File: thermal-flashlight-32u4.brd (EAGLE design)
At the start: 49.8 x 42.9 mm, 31 parts, among them IC1 ATMEGA328P, IC2 MCP73831, IC4 MCP1700-33, J1 AYZ0202, J2 1X2-3.5MM, Q4 BSS123, U1 MLX90614_, X1 USBSMD

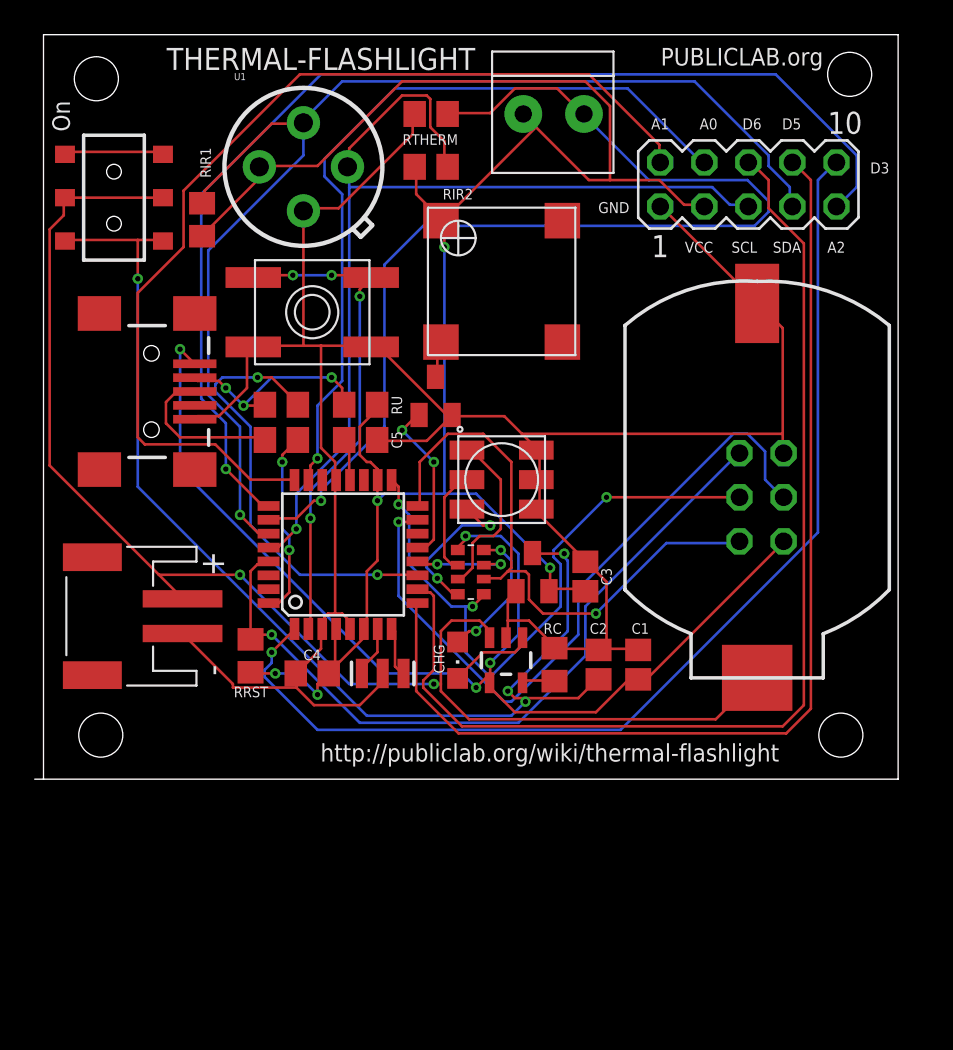
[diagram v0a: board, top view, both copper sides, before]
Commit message: added 32u4
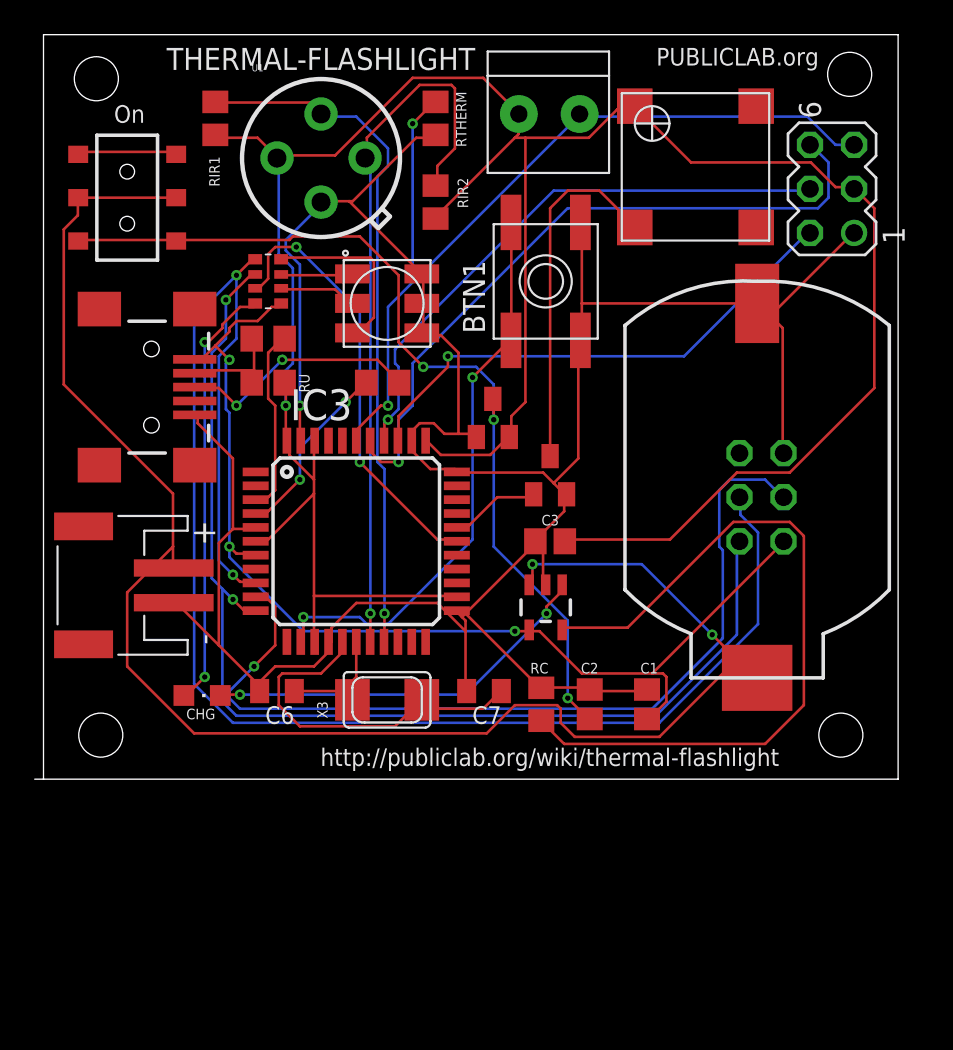
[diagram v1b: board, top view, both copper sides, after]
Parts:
- removed BTN: (no value), adafruit:EVQ-Q2
- removed C4, C5: 0.1uF, rcl:C0805
- removed IC1: ATMEGA328P, atmel:TQFP32-08
- removed RRST: 10k, rcl:R0805@1
- removed X: 12MHz, SparkFunNew:RESONATOR-SMD
- added BTN1: (no value), adafruit:EVQ-Q2
- added C6, C7: 18pF, adafruit:C0805K
- added IC3: ATMEGA32U4-AU, adaprog:TQFP44
- added X3: 8MHz, adaprog:NX5032
- SV1: device con-lstb:MA05-2 -> con-lstb:MA03-2
- moved RN1 20.4 mm to (13.2, 28.7), turned to 270 degrees
- moved CHG 14.9 mm to (9.40, 4.83), turned to 270 degrees
- moved U$1 13.0 mm to (37.8, 35.3)
- moved LED 12.1 mm to (20.1, 27.4)
- moved IC4 9.18 mm to (26.2, 20.8)
- moved Q4 8.03 mm to (29.5, 17.5)
- moved RD+ 6.71 mm to (19.8, 22.9), turned to 180 degrees
- moved RIR1 5.89 mm to (10.2, 38.1)
- moved RU 5.48 mm to (13.2, 22.9)
- moved SV1 4.83 mm to (45.7, 34.0), turned to 90 degrees
- moved RD- 3.89 mm to (13.2, 25.4)
- moved IC2 3.81 mm to (29.2, 9.91)
- moved C3 2.87 mm to (29.5, 13.7), turned to 180 degrees
- moved RC 2.41 mm to (29.0, 4.32)
- moved C1 2.34 mm to (35.1, 4.32)
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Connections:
- removed net AREF: C5.2, IC1.20
- removed net D10: IC1.14
- removed net D2: IC1.32, RD+.2
- removed net D3: IC1.1, SV1.10
- removed net D4: BTN.B, BTN.B', IC1.2
- removed net D5: IC1.9, SV1.8
- removed net D6: IC1.10, SV1.6
- removed net N$12: IC1.19
- removed net N$13: IC1.22
- removed net N$2: IC1.7, X.1
- removed net N$3: IC1.8, X.3
- removed net RXD: IC1.30
- removed net TXD: IC1.31
- new net A4: IC3.40
- new net A5: IC3.41
- new net D0/RX: IC3.20
- new net D1/TX: IC3.21
- new net D11: IC3.12
- new net D4_A6: IC3.25
- new net D6*: IC3.27
- new net IO10*: IC3.30
- new net IO12*: IC3.26
- new net N$11: IC3.4, RD+.2
- new net N$15: C7.1, IC3.16, X3.P$1
- new net N$16: C6.1, IC3.17, X3.P$2
- new net N$18: IC3.3, RD-.2
- new net PC6: IC3.31
- new net PC7: IC3.32
- new net RST: BTN1.B, BTN1.B', IC3.13
- new net RXLED/SS: IC3.8
- new net TXLED: IC3.22
- net A0: now also IC3.36, SV1.2; no longer IC1.23, SV1.4
- net A1: now also IC3.37, SV1.4; no longer IC1.24, SV1.2
- net A2: now also IC3.38, SV1.6; no longer IC1.25, SV1.9
- net A3: now also IC3.39, SV1.5; no longer IC1.26
- net D7: now also IC3.1; no longer IC1.11, RD-.2
- net D8: now also IC3.28; no longer IC1.12
- net D9: now also IC3.29; no longer IC1.13
- net GND: now also BTN1.A, BTN1.A', C6.2, C7.2, IC3.15, IC3.23, IC3.33, IC3.35, IC3.43, IC3.5; no longer BTN.A, BTN.A', C4.1, C5.1, IC1.21, IC1.3, IC1.5, X.2
- net MISO: now also IC3.11; no longer IC1.16
- net MOSI: now also IC3.10; no longer IC1.15
- net RESET: no longer IC1.29, RRST.1
- net SCK: now also IC3.9; no longer IC1.17
- net SCL: now also IC3.18; no longer IC1.28, SV1.5
- net SDA: now also IC3.19; no longer IC1.27, SV1.7
- net VBUS: now also IC3.7
- net VCC: now also IC3.14, IC3.24, IC3.34, IC3.42, IC3.44, IC3.6; no longer C4.2, IC1.18, IC1.4, IC1.6, RRST.2
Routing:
- net D3: track 63.2 -> 0.00 mm, vias 1 -> 0
- net D6: track 62.7 -> 0.00 mm
- net D5: track 61.4 -> 0.00 mm
- net SCK: track 36.5 -> 89.2 mm, vias 3 -> 2
- net RESET: track 43.7 -> 0.00 mm, vias 1 -> 0
- net N$6: track 1.90 -> 43.2 mm
- net VCC: track 115.3 -> 153.7 mm, vias 5 -> 1
- net RST: track 0.00 -> 32.8 mm, vias 0 -> 2
- net MISO: track 34.1 -> 65.9 mm, vias 1 -> 2
- net SDA: track 69.1 -> 40.1 mm
- net D4: track 28.8 -> 0.00 mm, vias 4 -> 0
- net A2: track 65.9 -> 40.0 mm
- net D7: track 25.4 -> 0.00 mm, vias 2 -> 0
- net GND: track 142.3 -> 167.3 mm, vias 0 -> 1
- net A1: track 58.3 -> 33.4 mm, vias 0 -> 1
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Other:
- board text removed: "A0"
- board text removed: "A1"
- board text removed: "A2"
- board text removed: "D3"
- board text removed: "D5"
- board text removed: "D6"
- board text removed: "GND"
- board text removed: "SCL"
- board text removed: "SDA"
- board text removed: "VCC"

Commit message: update
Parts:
- renumbered BTN1 to BTN
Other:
- board text added: "buzzer"
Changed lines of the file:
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@@
 <circle x="46.736" y="40.64" radius="1.27" width="0.002540625" layer="20"/>
 <circle x="46.228" y="2.54" radius="1.27" width="0.002540625" layer="20"/>
+<text x="40.386" y="35.052" size="0.8128" layer="25" ratio="20" rot="R180">buzzer</text>
 </plain>
 <attributes>
@@
 <element name="C7" library="adafruit" package="C0805K" value="18pF" x="25.654" y="5.08" rot="R180"/>
 <element name="IC3" library="adaprog" package="TQFP44" value="ATMEGA32U4-AU" x="18.288" y="13.716"/>
-<element name="BTN1" library="adafruit" package="EVQ-Q2" value="" x="29.21" y="28.702" rot="R90"/>
+<element name="BTN" library="adafruit" package="EVQ-Q2" value="" x="29.21" y="28.702" smashed="yes" rot="R90">
+<attribute name="NAME" x="25.71" y="25.702" size="0.8128" layer="25" rot="R90"/>
+<attribute name="VALUE" x="34.01" y="25.502" size="1.27" layer="27" rot="R90"/>
+</element>
 <element name="SV1" library="con-lstb" package="MA03-2" value="" x="45.72" y="34.036" smashed="yes" rot="R90">
 <attribute name="OC_NEWARK" value="unknown" x="45.72" y="34.036" size="1.778" layer="27" rot="R90" display="off"/>
@@
 <contactref element="C7" pad="2"/>
 <contactref element="IC3" pad="33"/>
-<contactref element="BTN1" pad="A'"/>
-<contactref element="BTN1" pad="A"/>
+<contactref element="BTN" pad="A'"/>
+<contactref element="BTN" pad="A"/>
 <contactref element="SV1" pad="1"/>
 <wire x1="31.2928" y1="31.9024" x2="31.2928" y2="27.432" width="0.1524" layer="1"/>
@@
 <signal name="RST">
 <contactref element="IC3" pad="13"/>
-<contactref element="BTN1" pad="B"/>
-<contactref element="BTN1" pad="B'"/>
+<contactref element="BTN" pad="B"/>
+<contactref element="BTN" pad="B'"/>
 <wire x1="15.24" y1="9.3472" x2="15.24" y2="7.9248" width="0.1524" layer="1"/>
 <wire x1="18.4912" y1="9.3472" x2="15.24" y2="9.3472" width="0.1524" layer="16"/>

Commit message: update
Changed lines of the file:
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@@
 <text x="42.672" y="1.778" size="1.016" layer="25" ratio="20" rot="R180">http://publiclab.org/wiki/thermal-flashlight</text>
 <text x="25.146" y="42.164" size="1.27" layer="25" ratio="20" rot="R180">THERMAL-FLASHLIGHT</text>
-<text x="44.958" y="42.164" size="1.016" layer="25" ratio="20" rot="R180">PUBLICLAB.org</text>
+<text x="44.704" y="41.91" size="1.016" layer="25" ratio="20" rot="R180">PUBLICLAB.org</text>
 <wire x1="49.53" y1="0" x2="0.254" y2="0" width="0" layer="20"/>
 <wire x1="0.254" y1="0" x2="-0.254" y2="0" width="0" layer="20"/>

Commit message: update
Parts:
- added LED1: RGBLED5050, adafruit:RGBLED5050
- added RN2: (no value), resistor-dil:EXB38V
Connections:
- new net N$12: LED1.2, RN2.6
- new net N$2: LED1.3, RN2.8
- new net N$3: LED1.1, RN2.7
- net A3: no longer J2.2, RTHERM.2
- net A4: now also J2.2, RTHERM.2
- net D8: now also RN2.3
- net GND: now also LED1.4, LED1.5, LED1.6
- net MISO: now also RN2.2
- net SCK: now also RN2.1
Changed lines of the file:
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@@
 <attribute name="VALUE" x="49.911" y="32.766" size="1.27" layer="27" ratio="10" rot="R90"/>
+</element>
+<element name="LED1" library="adafruit" package="RGBLED5050" value="RGBLED5050" x="3.048" y="-4.826"/>
+<element name="RN2" library="resistor-dil" package="EXB38V" value="" x="2.286" y="-12.446">
+<attribute name="OC_NEWARK" value="unknown" x="-6.35" y="-3.048" size="1.778" layer="27" display="off"/>
+<attribute name="MPN" value="" x="-6.35" y="-3.048" size="1.778" layer="27" display="off"/>
+<attribute name="MF" value="" x="-6.35" y="-3.048" size="1.778" layer="27" display="off"/>
+<attribute name="OC_FARNELL" value="unknown" x="-6.35" y="-3.048" size="1.778" layer="27" display="off"/>
 </element>
 </elements>
@@
 <wire x1="31.0896" y1="25.1968" x2="31.21" y2="25.302" width="0.1524" layer="1"/>
 <via x="15.0368" y="21.5392" extent="1-16" drill="0.3048"/>
+<contactref element="LED1" pad="4"/>
+<contactref element="LED1" pad="6"/>
+<contactref element="LED1" pad="5"/>
+<wire x1="5.048" y1="-3.126" x2="12.5984" y2="5.08" width="0" layer="19" extent="1-1"/>
+<wire x1="5.048" y1="-4.826" x2="5.048" y2="-3.126" width="0" layer="19" extent="1-1"/>
+<wire x1="5.048" y1="-6.526" x2="5.048" y2="-4.826" width="0" layer="19" extent="1-1"/>
 </signal>
 <signal name="VBUS">
@@
 <contactref element="RIR1" pad="2"/>
 <contactref element="RIR2" pad="2"/>
-<contactref element="J2" pad="1"/>
 <contactref element="IC3" pad="14"/>
 <contactref element="IC3" pad="34"/>
@@
 <wire x1="27.6352" y1="38.2016" x2="27.6352" y2="37.1856" width="0.1524" layer="1"/>
 <wire x1="22.9616" y1="32.512" x2="22.86" y2="32.324" width="0.1524" layer="1"/>
-<wire x1="27.6352" y1="38.2016" x2="27.664" y2="38.354" width="0.1524" layer="1"/>
 <wire x1="33.3248" y1="38.608" x2="34.3408" y2="38.608" width="0.1524" layer="1"/>
 <wire x1="31.6992" y1="36.9824" x2="33.3248" y2="38.608" width="0.1524" layer="1"/>
@@
 <wire x1="27.6352" y1="38.4048" x2="25.6032" y2="40.4368" width="0.1524" layer="1"/>
 <wire x1="13.8176" y1="35.9664" x2="13.716" y2="35.814" width="0.1524" layer="1"/>
-<wire x1="27.6352" y1="38.4048" x2="27.664" y2="38.354" width="0.1524" layer="1"/>
 <wire x1="14.224" y1="23.5712" x2="14.224" y2="21.5392" width="0.1524" layer="16"/>
 <wire x1="14.6304" y1="23.9776" x2="14.224" y2="23.5712" width="0.1524" layer="16"/>
@@
 <wire x1="46.9392" y1="34.1376" x2="46.99" y2="34.036" width="0.1524" layer="1"/>
 <via x="14.224" y="21.5392" extent="1-16" drill="0.3048"/>
+<contactref element="J2" pad="1"/>
+<wire x1="27.6352" y1="38.4048" x2="27.664" y2="38.354" width="0" layer="19" extent="1-1"/>
+<wire x1="27.6352" y1="38.2016" x2="27.664" y2="38.354" width="0" layer="19" extent="1-1"/>
 </signal>
 <signal name="SCK">
@@
 <via x="11.3792" y="29.0576" extent="1-16" drill="0.3048"/>
 <via x="11.176" y="11.7856" extent="1-16" drill="0.3048"/>
+<contactref element="RN2" pad="1"/>
+<wire x1="1.011" y1="-13.196" x2="11.176" y2="3.2512" width="0" layer="19" extent="1-16"/>
 </signal>
 <signal name="MISO">
@@
 <via x="10.7696" y="27.6352" extent="1-16" drill="0.3048"/>
 <via x="11.176" y="10.3632" extent="1-16" drill="0.3048"/>
+<contactref element="RN2" pad="2"/>
+<wire x1="1.886" y1="-13.196" x2="11.3792" y2="3.6576" width="0" layer="19" extent="1-16"/>
 </signal>
 <signal name="MOSI">
@@
 </signal>
 <signal name="A3">
-<contactref element="J2" pad="2"/>
-<contactref element="RTHERM" pad="2"/>
 <contactref element="IC3" pad="39"/>
 <contactref element="SV1" pad="5"/>
@@
 <wire x1="31.0896" y1="38.2016" x2="21.5392" y2="28.6512" width="0.1524" layer="16"/>
 <wire x1="21.5392" y1="28.6512" x2="20.1168" y2="27.2288" width="0.1524" layer="16"/>
-<wire x1="31.0896" y1="38.2016" x2="31.164" y2="38.354" width="0.1524" layer="16"/>
 <wire x1="21.5392" y1="37.7952" x2="22.7584" y2="39.0144" width="0.1524" layer="1"/>
 <wire x1="21.5392" y1="28.6512" x2="21.5392" y2="37.7952" width="0.1524" layer="16"/>
-<wire x1="22.7584" y1="39.0144" x2="22.86" y2="39.05" width="0.1524" layer="1"/>
 <wire x1="45.9232" y1="36.576" x2="46.99" y2="36.576" width="0.1524" layer="16"/>
 <wire x1="44.2976" y1="38.2016" x2="45.9232" y2="36.576" width="0.1524" layer="16"/>
 <wire x1="31.2928" y1="38.2016" x2="44.2976" y2="38.2016" width="0.1524" layer="16"/>
-<wire x1="31.2928" y1="38.2016" x2="31.164" y2="38.354" width="0.1524" layer="16"/>
 <via x="20.1168" y="21.5392" extent="1-16" drill="0.3048"/>
 <via x="21.5392" y="37.7952" extent="1-16" drill="0.3048"/>
+<wire x1="31.0896" y1="38.2016" x2="31.2928" y2="38.2016" width="0" layer="19" extent="16-16"/>
 </signal>
 <signal name="D8">
@@
 <via x="14.8336" y="30.6832" extent="1-16" drill="0.3048"/>
 <via x="18.4912" y="18.288" extent="1-16" drill="0.3048"/>
+<contactref element="RN2" pad="3"/>
+<wire x1="2.686" y1="-13.196" x2="22.9616" y2="13.8176" width="0" layer="19" extent="1-1"/>
 </signal>
 <signal name="A1">
@@
 <signal name="A4">
 <contactref element="IC3" pad="40"/>
+<contactref element="RTHERM" pad="2"/>
+<contactref element="J2" pad="2"/>
+<wire x1="22.86" y1="39.05" x2="31.164" y2="38.354" width="0" layer="19" extent="1-1"/>
+<wire x1="17.488" y1="19.516" x2="22.86" y2="39.05" width="0" layer="19" extent="1-1"/>
 </signal>
 <signal name="A5">
@@
 <contactref element="IC3" pad="25"/>
 </signal>
+<signal name="N$2">
+<contactref element="LED1" pad="3"/>
+<contactref element="RN2" pad="8"/>
+<wire x1="1.048" y1="-6.526" x2="1.011" y2="-11.696" width="0" layer="19" extent="1-1"/>
+</signal>
+<signal name="N$3">
+<contactref element="LED1" pad="1"/>
+<contactref element="RN2" pad="7"/>
+<wire x1="1.048" y1="-3.126" x2="1.886" y2="-11.696" width="0" layer="19" extent="1-1"/>
+</signal>
+<signal name="N$12">
+<contactref element="LED1" pad="2"/>
+<contactref element="RN2" pad="6"/>
+<wire x1="1.048" y1="-4.826" x2="2.686" y2="-11.696" width="0" layer="19" extent="1-1"/>
+</signal>
 </signals>
